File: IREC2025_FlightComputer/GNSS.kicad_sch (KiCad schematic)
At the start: 1 part, among them U8 SAM-M10Q-00B

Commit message: update
21/3/2025
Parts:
- added BT1: Battery, Battery:BatteryHolder_Seiko_MS621F, symbol Device:Battery
- added C71: 1uF, PCM_JLCPCB:C_0402, symbol PCM_JLCPCB-Capacitors:0402,1uF
- added D6: PMEG2005EJ, Diode_SMD:D_SOD-323F, symbol Diode:PMEG2005EJ
- added LED1, LED2: HS-0402-UR, EasyEDA:LED0402-R-RD, symbol EasyEDA:HS-0402-UR
- added R33, R34: 470Ω, PCM_JLCPCB:R_0402, symbol PCM_JLCPCB-Resistors:0402,470Ω
- added R35, R36: 1kΩ, PCM_JLCPCB:R_0402, symbol PCM_JLCPCB-Resistors:0402,1kΩ
- added R37: 3.3kΩ, PCM_JLCPCB:R_0402, symbol PCM_JLCPCB-Resistors:0402,3.3kΩ
- renumbered U8 to U18
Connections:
- net GND: now also BT1.2 (-), C71.2, LED1.2 (-), LED2.2 (-)
- net at U18.13 (TXD): now also R34.1
- net at U18.14 (RXD): now also R33.1
- net +3V3: now reaches U18.17 (VCC)
- net +3V3: now also U18.2 (V_IO), D6.2 (A), R36.1
- net GNSS_RST: now reaches U18.18 (RESET_N)
- net GNSS_INT: now reaches U18.19 (EXTINT)
- net Backup: now reaches U18.3 (V_BCKP)
- net Backup: now also BT1.1 (+), C71.1, R37.2
- net PPS: now reaches U18.7 (TIMEPULSE)
- net PPS: now also R35.1
- net GNSS_SAFEBOOT: now reaches U18.8 (SAFEBOOT_N)
- new net: D6.1 (K), R37.1
- new net: LED2.1 (+), R36.2
- new net: LED1.1 (+), R35.2
- new net GNSS_RX: R33.2
- new net GNSS_TX: R34.2
- no-connect marks 0 -> 2
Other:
- note added: "Backup Battery"
- note added: "GNSS Module"
- note added: "LED indicators"
- moved on the sheet: U18

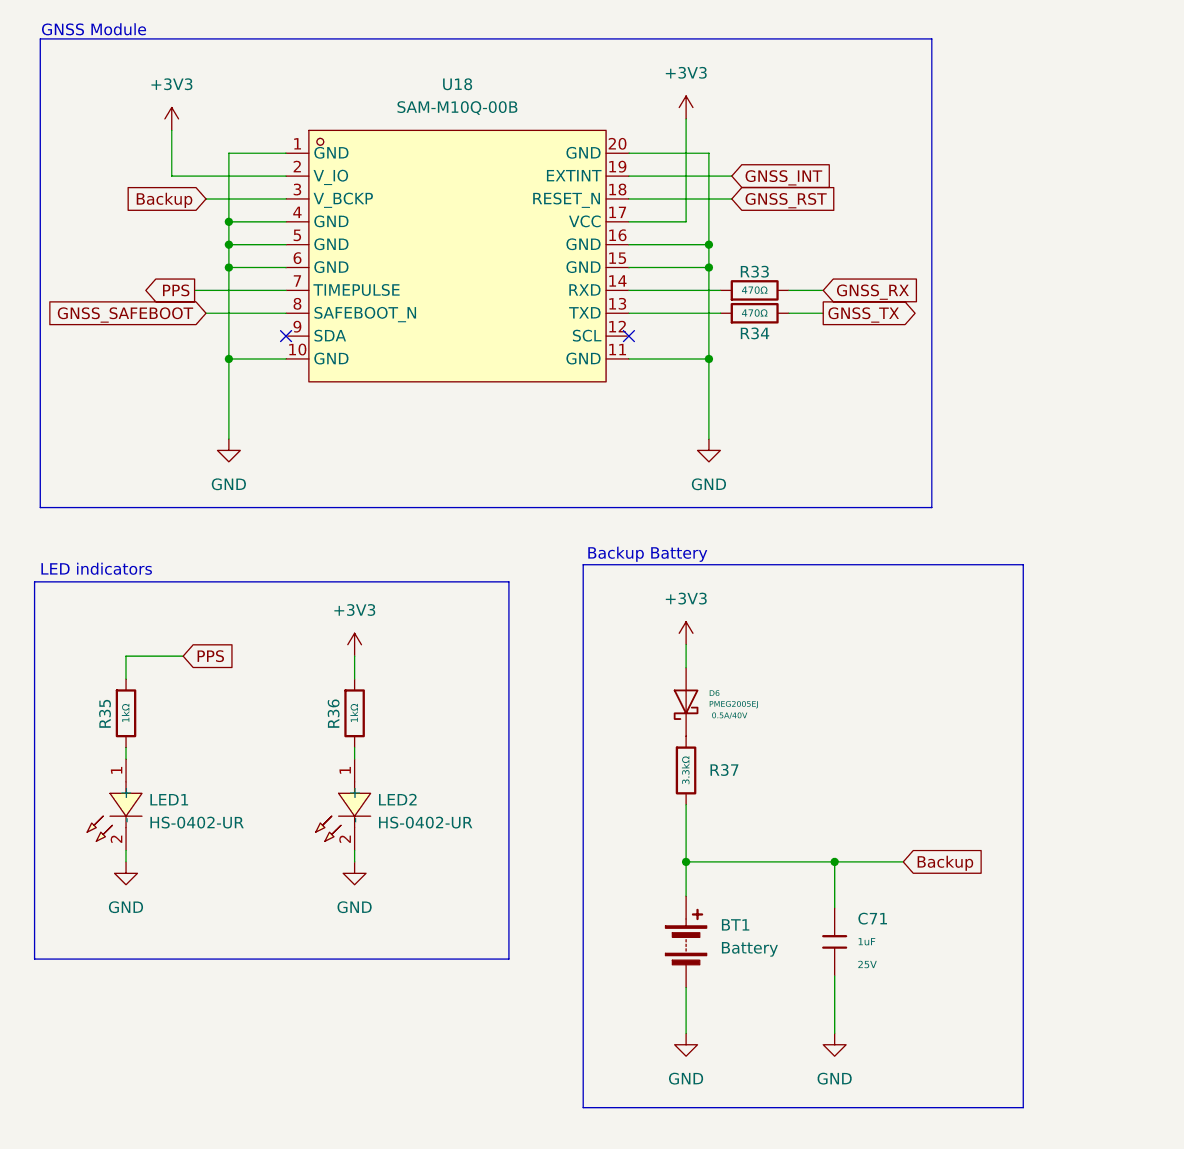
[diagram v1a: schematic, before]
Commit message: Updated schematic + initiate layout
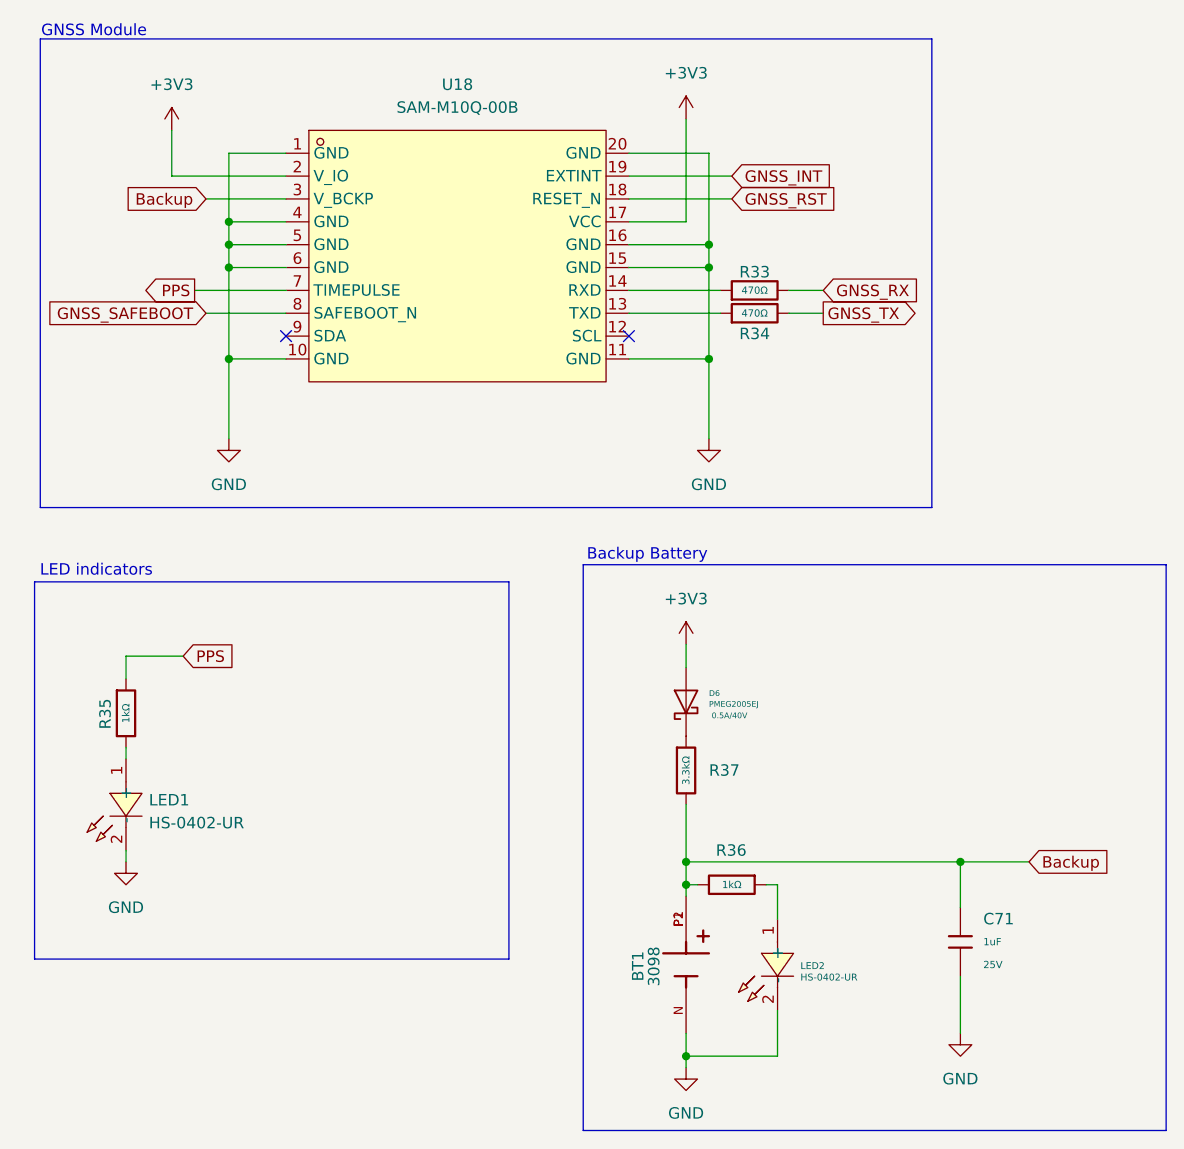
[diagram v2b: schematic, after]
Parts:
- removed BT1: Battery, Battery:BatteryHolder_Seiko_MS621F, symbol Device:Battery
- added BT1: 3098, GNSS:BAT_3098, symbol Battery3V_holder:3098
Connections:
- net +3V3: no longer R36.1
- net Backup: now also R36.2, BT1.P1, BT1.P2
- net GND: now also BT1.N
- net at LED2.1 (+): now also R36.1; no longer R36.2
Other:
- moved on the sheet: C71, LED2, R36

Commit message: checkpoint
before the great layout change
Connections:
- net +3V3 renamed +3.3V
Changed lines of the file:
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@@
 	)
 	(symbol
-		(lib_id "power:+3V3")
+		(lib_id "power:+3.3V")
 		(at 35.56 29.21 0)
 		(unit 1)
@@
 		(dnp no)
 		(fields_autoplaced yes)
-		(property "Reference" "#PWR098"
+		(property "Reference" "#PWR093"
 			(at 35.56 33.02 0)
 			(effects
@@
 			)
 		)
-		(property "Value" "+3V3"
+		(property "Value" "+3.3V"
 			(at 35.56 24.13 0)
 			(effects
@@
 			)
 		)
-		(property "Description" "Power symbol creates a global label with name \"+3V3\""
+		(property "Description" "Power symbol creates a global label with name \"+3.3V\""
 			(at 35.56 29.21 0)
 			(effects
@@
 			(project "IREC2025_FlightComputer"
 				(path "/d402aac1-6798-4745-a2ce-fc3f8e4c9afb/405b4b98-de6a-459e-bdcd-313bf0eeb515"
-					(reference "#PWR098")
+					(reference "#PWR093")
 					(unit 1)
 				)
@@
 	)
 	(symbol
-		(lib_id "power:+3V3")
-		(at 92.71 27.94 0)
-		(unit 1)
-		(exclude_from_sim no)
-		(in_bom yes)
-		(on_board yes)
-		(dnp no)
-		(fields_autoplaced yes)
-		(property "Reference" "#PWR097"
-			(at 92.71 31.75 0)
-			(effects
-				(font
-					(size 1.27 1.27)
-				)
-				(hide yes)
-			)
-		)
-		(property "Value" "+3V3"
-			(at 92.71 22.86 0)
-			(effects
-				(font
-					(size 1.27 1.27)
-				)
-			)
-		)
-		(property "Footprint" ""
-			(at 92.71 27.94 0)
-			(effects
-				(font
-					(size 1.27 1.27)
-				)
-				(hide yes)
-			)
-		)
-		(property "Datasheet" ""
-			(at 92.71 27.94 0)
-			(effects
-				(font
-					(size 1.27 1.27)
-				)
-				(hide yes)
-			)
-		)
-		(property "Description" "Power symbol creates a global label with name \"+3V3\""
-			(at 92.71 27.94 0)
-			(effects
-				(font
-					(size 1.27 1.27)
-				)
-				(hide yes)
-			)
-		)
-		(pin "1"
-		)
-		(instances
-			(project ""
-				(path "/d402aac1-6798-4745-a2ce-fc3f8e4c9afb/405b4b98-de6a-459e-bdcd-313bf0eeb515"
-					(reference "#PWR097")
-					(unit 1)
-				)
-			)
-		)
-	)
-	(symbol
 		(lib_id "PCM_JLCPCB-Resistors:0402,1kΩ")
 		(at 97.79 113.03 270)
@@
 	)
 	(symbol
+		(lib_id "power:+3.3V")
+		(at 92.71 27.94 0)
+		(unit 1)
+		(exclude_from_sim no)
+		(in_bom yes)
+		(on_board yes)
+		(dnp no)
+		(fields_autoplaced yes)
+		(property "Reference" "#PWR094"
+			(at 92.71 31.75 0)
+			(effects
+				(font
+					(size 1.27 1.27)
+				)
+				(hide yes)
+			)
+		)
+		(property "Value" "+3.3V"
+			(at 92.71 22.86 0)
+			(effects
+				(font
+					(size 1.27 1.27)
+				)
+			)
+		)
+		(property "Footprint" ""
+			(at 92.71 27.94 0)
+			(effects
+				(font
+					(size 1.27 1.27)
+				)
+				(hide yes)
+			)
+		)
+		(property "Datasheet" ""
+			(at 92.71 27.94 0)
+			(effects
+				(font
+					(size 1.27 1.27)
+				)
+				(hide yes)
+			)
+		)
+		(property "Description" "Power symbol creates a global label with name \"+3.3V\""
+			(at 92.71 27.94 0)
+			(effects
+				(font
+					(size 1.27 1.27)
+				)
+				(hide yes)
+			)
+		)
+		(pin "1"
+		)
+		(instances
+			(project "IREC2025_FlightComputer"
+				(path "/d402aac1-6798-4745-a2ce-fc3f8e4c9afb/405b4b98-de6a-459e-bdcd-313bf0eeb515"
+					(reference "#PWR094")
+					(unit 1)
+				)
+			)
+		)
+	)
+	(symbol
 		(lib_id "power:GND")
 		(at 95.25 63.5 0)
@@
 	)
 	(symbol
-		(lib_id "power:+3V3")
-		(at 92.71 86.36 0)
-		(unit 1)
-		(exclude_from_sim no)
-		(in_bom yes)
-		(on_board yes)
-		(dnp no)
-		(fields_autoplaced yes)
-		(property "Reference" "#PWR0101"
-			(at 92.71 90.17 0)
-			(effects
-				(font
-					(size 1.27 1.27)
-				)
-				(hide yes)
-			)
-		)
-		(property "Value" "+3V3"
-			(at 92.71 81.28 0)
-			(effects
-				(font
-					(size 1.27 1.27)
-				)
-			)
-		)
-		(property "Footprint" ""
-			(at 92.71 86.36 0)
-			(effects
-				(font
-					(size 1.27 1.27)
-				)
-				(hide yes)
-			)
-		)
-		(property "Datasheet" ""
-			(at 92.71 86.36 0)
-			(effects
-				(font
-					(size 1.27 1.27)
-				)
-				(hide yes)
-			)
-		)
-		(property "Description" "Power symbol creates a global label with name \"+3V3\""
-			(at 92.71 86.36 0)
-			(effects
-				(font
-					(size 1.27 1.27)
-				)
-				(hide yes)
-			)
-		)
-		(pin "1"
-		)
-		(instances
-			(project "IREC2025_FlightComputer"
-				(path "/d402aac1-6798-4745-a2ce-fc3f8e4c9afb/405b4b98-de6a-459e-bdcd-313bf0eeb515"
-					(reference "#PWR0101")
-					(unit 1)
-				)
-			)
-		)
-	)
-	(symbol
 		(lib_id "Battery3V_holder:3098")
 		(at 92.71 121.92 270)
@@
 					(unit 1)
 				)
+			)
+		)
+	)
+	(symbol
+		(lib_id "power:+3.3V")
+		(at 92.71 86.36 0)
+		(unit 1)
+		(exclude_from_sim no)
+		(in_bom yes)
+		(on_board yes)
+		(dnp no)
+		(fields_autoplaced yes)
+		(property "Reference" "#PWR092"
+			(at 92.71 90.17 0)
+			(effects
+				(font
+					(size 1.27 1.27)
+				)
+				(hide yes)
+			)
+		)
+		(property "Value" "+3.3V"
+			(at 92.71 81.28 0)
+			(effects
+				(font
+					(size 1.27 1.27)
+				)
+			)
+		)
+		(property "Footprint" ""
+			(at 92.71 86.36 0)
+			(effects
+				(font
+					(size 1.27 1.27)
+				)
+				(hide yes)
+			)
+		)
+		(property "Datasheet" ""
+			(at 92.71 86.36 0)
+			(effects
+				(font
+					(size 1.27 1.27)
+				)
+				(hide yes)
+			)
+		)
+		(property "Description" "Power symbol creates a global label with name \"+3.3V\""
+			(at 92.71 86.36 0)
+			(effects
+				(font
+					(size 1.27 1.27)
+				)
+				(hide yes)
+			)
+		)
+		(pin "1"
+		)
+		(instances
+			(project "IREC2025_FlightComputer"
+				(path "/d402aac1-6798-4745-a2ce-fc3f8e4c9afb/405b4b98-de6a-459e-bdcd-313bf0eeb515"
+					(reference "#PWR092")
+					(unit 1)
+				)

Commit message: 2 designs
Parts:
- renumbered C71 to C?, D6 to D?, LED1 to LED?, R35 to R?, R37 to R?, R33 to R?, U18 to U?
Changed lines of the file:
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@@
 		(on_board yes)
 		(dnp no)
-		(property "Reference" "D6"
+		(property "Reference" "D?"
 			(at 95.25 91.7574 90)
 			(effects
@@
 		)
 		(instances
-			(project ""
+			(project "IREC2025_FlightComputer"
 				(path "/d402aac1-6798-4745-a2ce-fc3f8e4c9afb/405b4b98-de6a-459e-bdcd-313bf0eeb515"
-					(reference "D6")
+					(reference "D?")
 					(unit 1)
 				)
@@
 		(dnp no)
 		(fields_autoplaced yes)
-		(property "Reference" "#PWR0103"
+		(property "Reference" "#PWR?"
 			(at 30.48 116.84 0)
 			(effects
@@
 		)
 		(instances
-			(project ""
+			(project "IREC2025_FlightComputer"
 				(path "/d402aac1-6798-4745-a2ce-fc3f8e4c9afb/405b4b98-de6a-459e-bdcd-313bf0eeb515"
-					(reference "#PWR0103")
+					(reference "#PWR?")
 					(unit 1)
 				)
@@
 		(on_board yes)
 		(dnp no)
-		(property "Reference" "R35"
+		(property "Reference" "R?"
 			(at 28.194 95.758 90)
 			(effects
@@
 		)
 		(instances
-			(project ""
+			(project "IREC2025_FlightComputer"
 				(path "/d402aac1-6798-4745-a2ce-fc3f8e4c9afb/405b4b98-de6a-459e-bdcd-313bf0eeb515"
-					(reference "R35")
+					(reference "R?")
 					(unit 1)
 				)
@@
 		(dnp no)
 		(fields_autoplaced yes)
-		(property "Reference" "R37"
+		(property "Reference" "R?"
 			(at 95.25 100.3299 0)
 			(effects
@@
 		)
 		(instances
-			(project ""
+			(project "IREC2025_FlightComputer"
 				(path "/d402aac1-6798-4745-a2ce-fc3f8e4c9afb/405b4b98-de6a-459e-bdcd-313bf0eeb515"
-					(reference "R37")
+					(reference "R?")
 					(unit 1)
 				)
@@
 		(dnp no)
 		(fields_autoplaced yes)
-		(property "Reference" "C71"
+		(property "Reference" "C?"
 			(at 125.73 116.8399 0)
 			(effects
@@
 		)
 		(instances
-			(project ""
+			(project "IREC2025_FlightComputer"
 				(path "/d402aac1-6798-4745-a2ce-fc3f8e4c9afb/405b4b98-de6a-459e-bdcd-313bf0eeb515"
-					(reference "C71")
+					(reference "C?")
 					(unit 1)
 				)
@@
 		(dnp no)
 		(fields_autoplaced yes)
-		(property "Reference" "#PWR099"
+		(property "Reference" "#PWR?"
 			(at 41.91 69.85 0)
 			(effects
@@
 		)
 		(instances
-			(project ""
+			(project "IREC2025_FlightComputer"
 				(path "/d402aac1-6798-4745-a2ce-fc3f8e4c9afb/405b4b98-de6a-459e-bdcd-313bf0eeb515"
-					(reference "#PWR099")
+					(reference "#PWR?")
 					(unit 1)
 				)
@@
 		(on_board yes)
 		(dnp no)
-		(property "Reference" "R33"
+		(property "Reference" "R?"
 			(at 100.33 44.958 90)
 			(effects
@@
 		)
 		(instances
-			(project ""
+			(project "IREC2025_FlightComputer"
 				(path "/d402aac1-6798-4745-a2ce-fc3f8e4c9afb/405b4b98-de6a-459e-bdcd-313bf0eeb515"
-					(reference "R33")
+					(reference "R?")
 					(unit 1)
 				)
@@
 		(dnp no)
 		(fields_autoplaced yes)
-		(property "Reference" "LED1"
+		(property "Reference" "LED?"
 			(at 33.02 103.6299 90)
 			(effects
@@
 		)
 		(instances
-			(project ""
+			(project "IREC2025_FlightComputer"
 				(path "/d402aac1-6798-4745-a2ce-fc3f8e4c9afb/405b4b98-de6a-459e-bdcd-313bf0eeb515"
-					(reference "LED1")
+					(reference "LED?")
 					(unit 1)
 				)
@@
 		(dnp no)
 		(fields_autoplaced yes)
-		(property "Reference" "U18"
+		(property "Reference" "U?"
 			(at 67.31 24.13 0)
 			(effects
@@
 		)
 		(instances
-			(project ""
+			(project "IREC2025_FlightComputer"
 				(path "/d402aac1-6798-4745-a2ce-fc3f8e4c9afb/405b4b98-de6a-459e-bdcd-313bf0eeb515"
-					(reference "U18")
+					(reference "U?")
 					(unit 1)
 				)

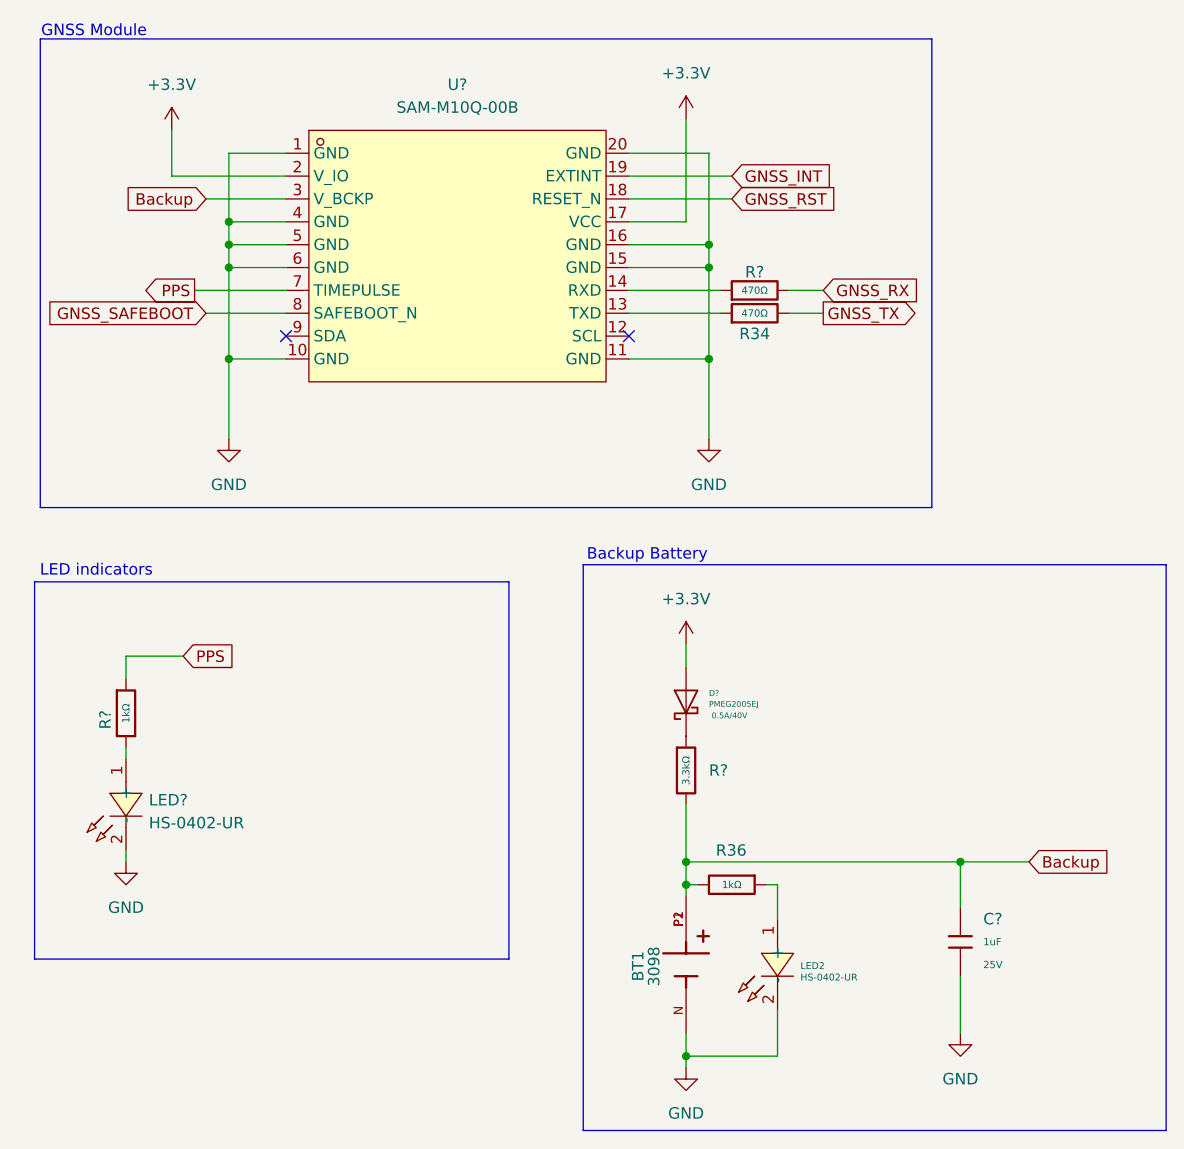
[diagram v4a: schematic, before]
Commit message: changed most resistors to 0603
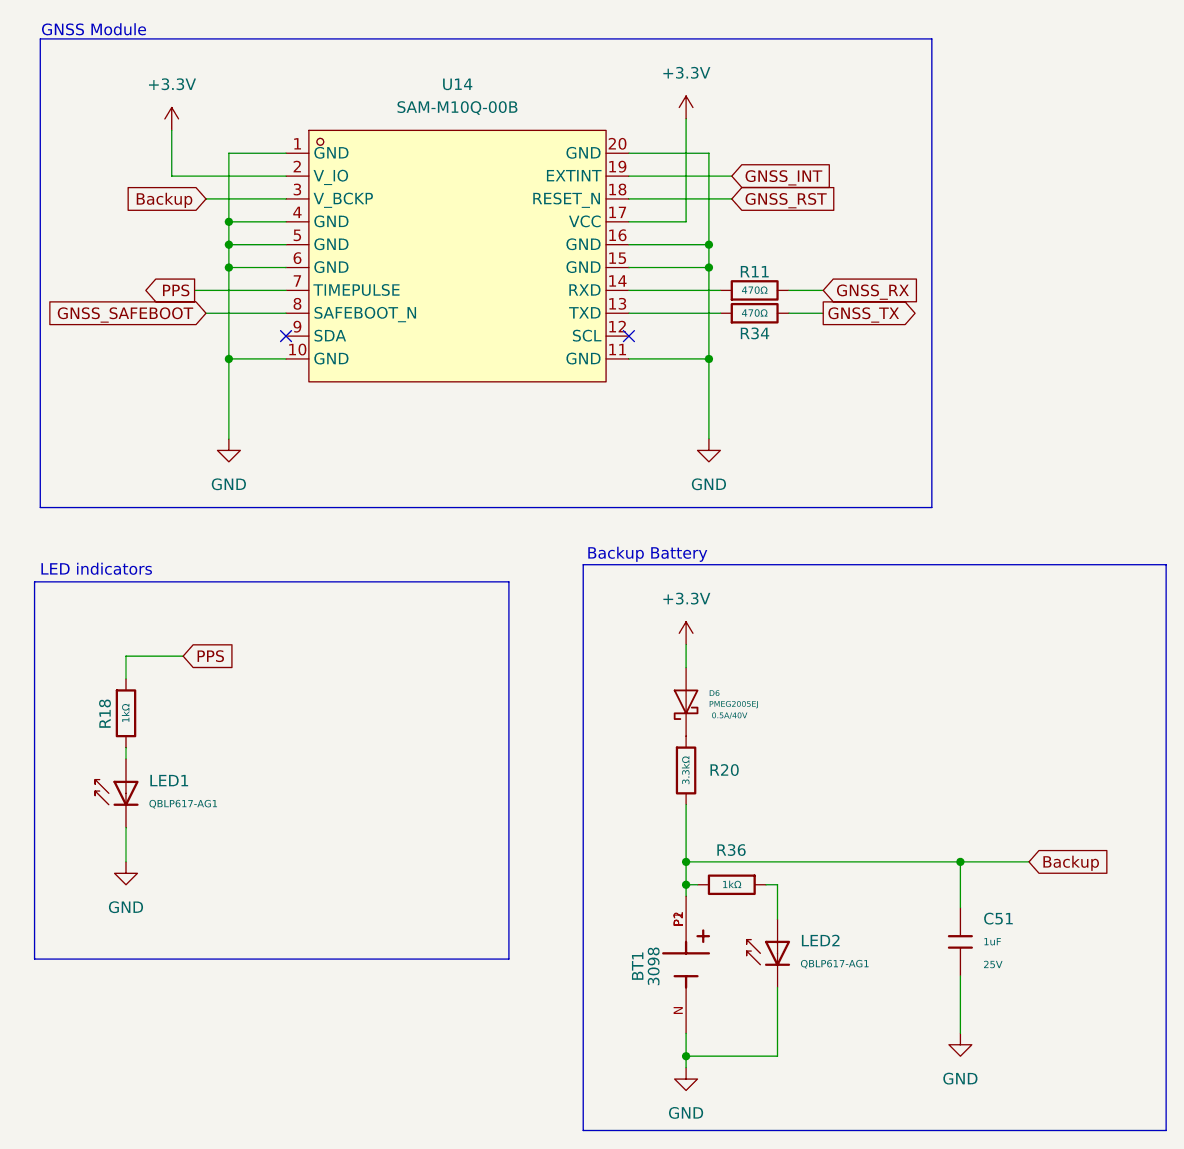
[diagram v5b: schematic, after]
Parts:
- removed LED2, LED?: HS-0402-UR, EasyEDA:LED0402-R-RD, symbol EasyEDA:HS-0402-UR
- added LED1, LED2: QBLP617-AG1, PCM_JLCPCB:D_0603, symbol PCM_JLCPCB-Diodes:LED,0603,Red
- R11, R18, R20: renamed from R?; footprint PCM_JLCPCB:R_0402 -> PCM_JLCPCB:R_0603
- R34, R36: footprint PCM_JLCPCB:R_0402 -> PCM_JLCPCB:R_0603
- gave numbers to parts that had none: 3
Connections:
- net GND: now also LED1.1, LED2.1
- net at R36.1: now also LED2.2
- net at R18.2: now also LED1.2
